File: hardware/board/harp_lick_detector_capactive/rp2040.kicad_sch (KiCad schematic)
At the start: 47 parts, among them J10 Conn_01x02_Male, J2 Conn_01x03_Male, J3 Conn_01x03_Male, J4 AudioJack3, U1 RP2040, U2 W25Q128JVS, U3 ADUM4160, U4 TPD2EUSB30, X1 ECS-TXO-2016

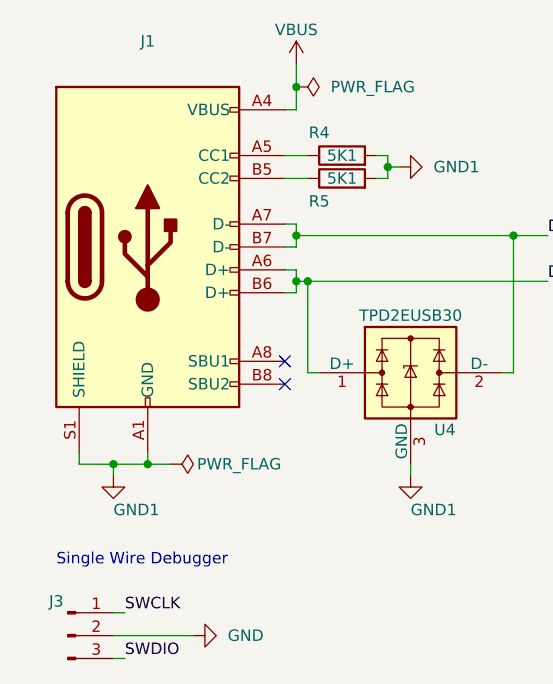
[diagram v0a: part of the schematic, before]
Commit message: add analog front end test board
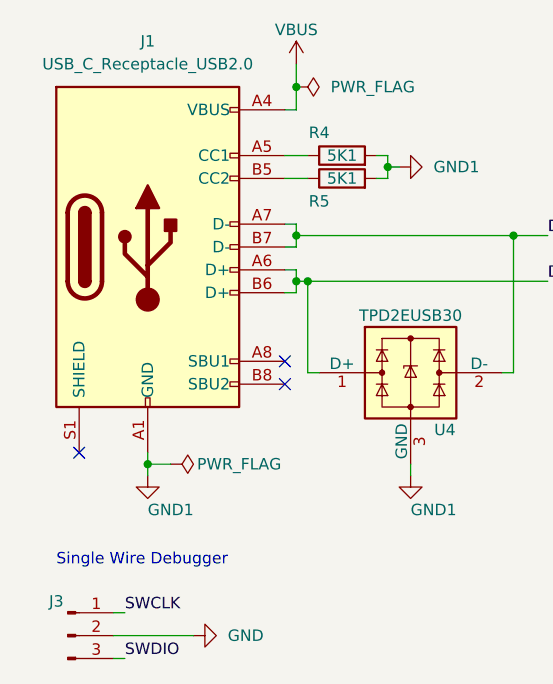
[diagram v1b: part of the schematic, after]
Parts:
- J1: value (none) -> USB_C_Receptacle_USB2.0; footprint (none) -> Connector_USB:USB_C_Receptacle_JAE_DX07S016JA1R1500
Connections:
- net GND1: no longer J1.S1 (SHIELD)
- no-connect marks 24 -> 25
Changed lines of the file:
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@@
   (junction (at 41.91 179.07) (diameter 0) (color 0 0 0 0)
   )
-  (junction (at 24.13 63.5) (diameter 0) (color 0 0 0 0)
-  )
   (junction (at 125.73 189.23) (diameter 0) (color 0 0 0 0)
   )
@@
   (no_connect (at 245.11 127))
   (no_connect (at 245.11 129.54))
+  (no_connect (at 20.32 62.23))
   (no_connect (at 245.11 144.78))
   (no_connect (at 245.11 147.32))
@@
     (stroke (width 0) (type default) (color 0 0 0 0))
   )
-  (wire (pts (xy 20.32 62.23) (xy 20.32 63.5))
-    (stroke (width 0) (type default) (color 0 0 0 0))
-  )
   (wire (pts (xy 31.75 177.8) (xy 31.75 180.34))
     (stroke (width 0) (type default) (color 0 0 0 0))
@@
     (stroke (width 0) (type default) (color 0 0 0 0))
   )
-  (wire (pts (xy 27.94 63.5) (xy 24.13 63.5))
-    (stroke (width 0) (type default) (color 0 0 0 0))
-  )
   (wire (pts (xy 195.58 54.61) (xy 195.58 55.88))
     (stroke (width 0) (type default) (color 0 0 0 0))
@@
     (stroke (width 0) (type default) (color 0 0 0 0))
   )
-  (wire (pts (xy 20.32 63.5) (xy 24.13 63.5))
-    (stroke (width 0) (type default) (color 0 0 0 0))
-  )
   (wire (pts (xy 38.1 147.32) (xy 29.21 147.32))
     (stroke (width 0) (type default) (color 0 0 0 0))
@@
     (stroke (width 0) (type default) (color 0 0 0 0))
   )
-  (wire (pts (xy 24.13 63.5) (xy 24.13 64.77))
+  (wire (pts (xy 27.94 63.5) (xy 27.94 64.77))
     (stroke (width 0) (type default) (color 0 0 0 0))
   )
@@
     (pin "2")
   )
-  (symbol (lib_id "power:GND1") (at 24.13 64.77 0) (unit 1)
+  (symbol (lib_id "power:GND1") (at 27.94 64.77 0) (unit 1)
     (in_bom yes) (on_board yes)
-    (property "Reference" "#PWR0131" (id 0) (at 24.13 71.12 0)
+    (property "Reference" "#PWR0131" (id 0) (at 27.94 71.12 0)
       (effects (font (size 1.27 1.27)) hide)
     )
-    (property "Value" "GND1" (id 1) (at 24.13 68.58 0)
+    (property "Value" "GND1" (id 1) (at 27.94 68.58 0)
       (effects (font (size 1.27 1.27)) (justify left))
     )
-    (property "Footprint" "" (id 2) (at 24.13 64.77 0)
+    (property "Footprint" "" (id 2) (at 27.94 64.77 0)
       (effects (font (size 1.27 1.27)) hide)
     )
-    (property "Datasheet" "" (id 3) (at 24.13 64.77 0)
+    (property "Datasheet" "" (id 3) (at 27.94 64.77 0)
       (effects (font (size 1.27 1.27)) hide)
     )
@@
     (in_bom yes) (on_board yes) (fields_autoplaced)
     (property "Reference" "J1" (id 0) (at 27.94 16.51 0))
-    (property "Value" "" (id 1) (at 27.94 19.05 0))
-    (property "Footprint" "" (id 2) (at 31.75 39.37 0)
+    (property "Value" "USB_C_Receptacle_USB2.0" (id 1) (at 27.94 19.05 0))
+    (property "Footprint" "Connector_USB:USB_C_Receptacle_JAE_DX07S016JA1R1500" (id 2) (at 31.75 39.37 0)
       (effects (font (size 1.27 1.27)) hide)
     )
